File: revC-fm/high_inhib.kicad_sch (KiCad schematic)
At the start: 9 parts, among them Q27 BSZ180P03NS3GATMA1, Q28 BSZ180P03NS3GATMA1, Q29 MMDT3946

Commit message: almost done!!!!!
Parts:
- Q27, Q28: value BSZ180P03NS3GATMA1 -> BSZ180
- R124: value 100k -> 220k
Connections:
- net IN_HI renamed IN
- net IN_LO renamed OUT
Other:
- note added: "High Side Inhibit"
- note added: "Push-Pull Gate Driver"
- moved on the sheet: C36, Q27, Q28, Q29A, Q29B, R120, R121, R122, R123, R124

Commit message: updated fab files
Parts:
- C36: Manufacturer (none) -> TDK; Mfr. Part No (none) -> CGA2B3X7R1H104K050BE
- Q16: renamed from Q27; Manufacturer (none) -> Infineon
- Q17: renamed from Q28; Manufacturer (none) -> Infineon
- Q18: renamed from Q29; Manufacturer (none) -> Diodes Incorporated
- R100: renamed from R123; Manufacturer (none) -> Stackpole Electronics; Mfr. Part No (none) -> RMCF0402FT1M00
- R101: renamed from R124; Manufacturer (none) -> Stackpole Electronics; Mfr. Part No (none) -> RMCF0402FT220K
- R97: renamed from R120; Manufacturer (none) -> Panasonic; Mfr. Part No (none) -> ERJ-2GEJ102X
- R98: renamed from R121; Manufacturer (none) -> Panasonic; Mfr. Part No (none) -> ERJ-2GEJ102X
- R99: renamed from R122; Manufacturer (none) -> Stackpole Electronics; Mfr. Part No (none) -> RMCF0603ZT0R00

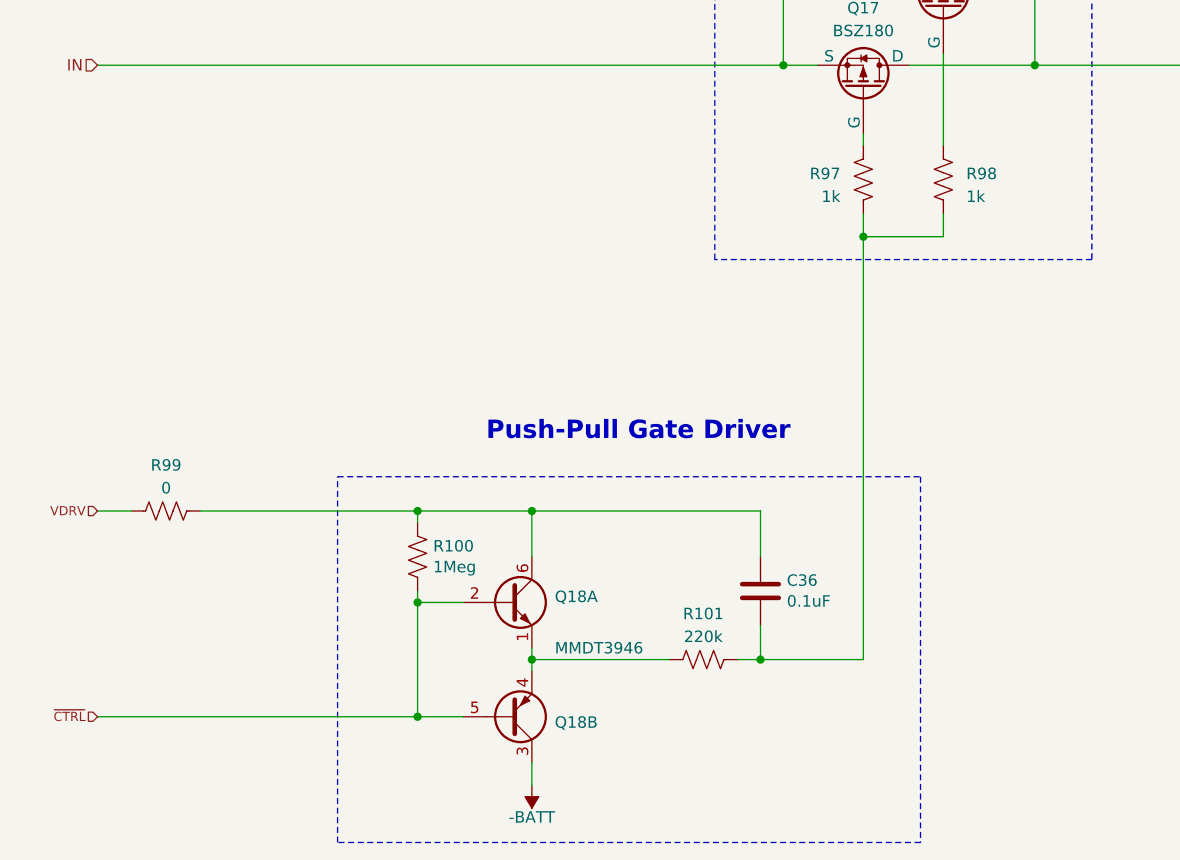
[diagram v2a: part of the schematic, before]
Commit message: updated per review, improved docs
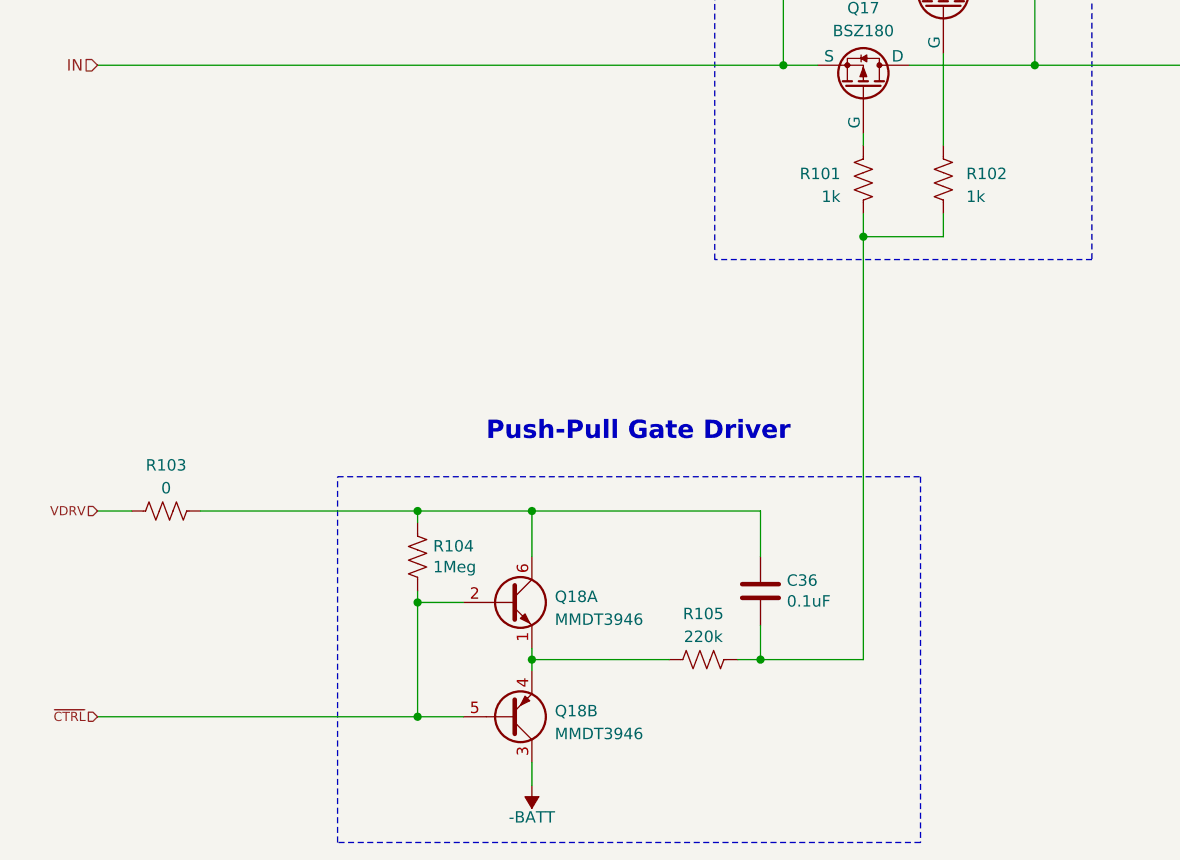
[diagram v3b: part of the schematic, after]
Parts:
- renumbered R97 to R101, R98 to R102, R99 to R103, R100 to R104, R101 to R105
